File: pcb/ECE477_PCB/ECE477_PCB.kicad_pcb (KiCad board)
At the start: 2 copper layers, 65 x 30 mm, 102 parts, among them J1 DEBUG, J10 ToF 5, J11 Pi Zero, J2 USB_B_Micro, J3 ESC, J4 ELRS, J5 AUX_PWR, J6 ToF 1, J7 ToF 2, J8 ToF 3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

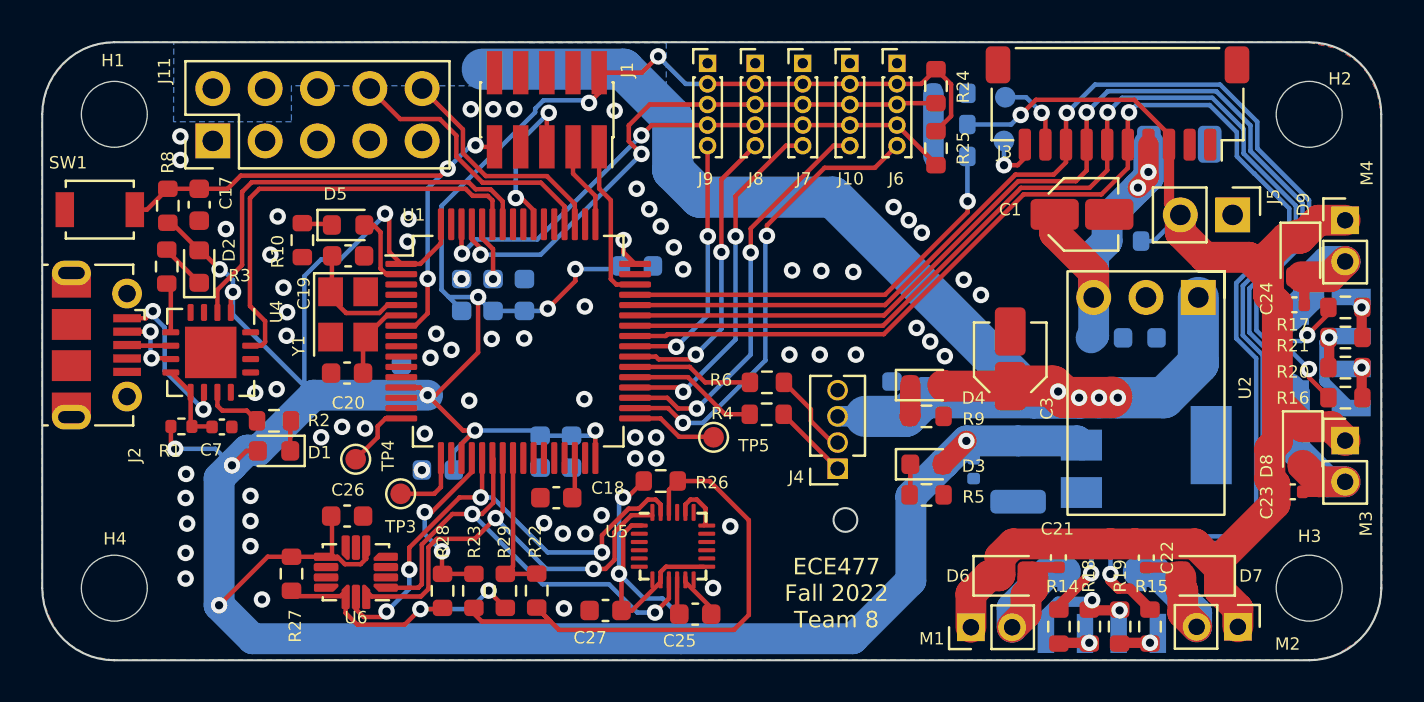
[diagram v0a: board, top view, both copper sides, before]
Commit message: committing before large change to FTDI
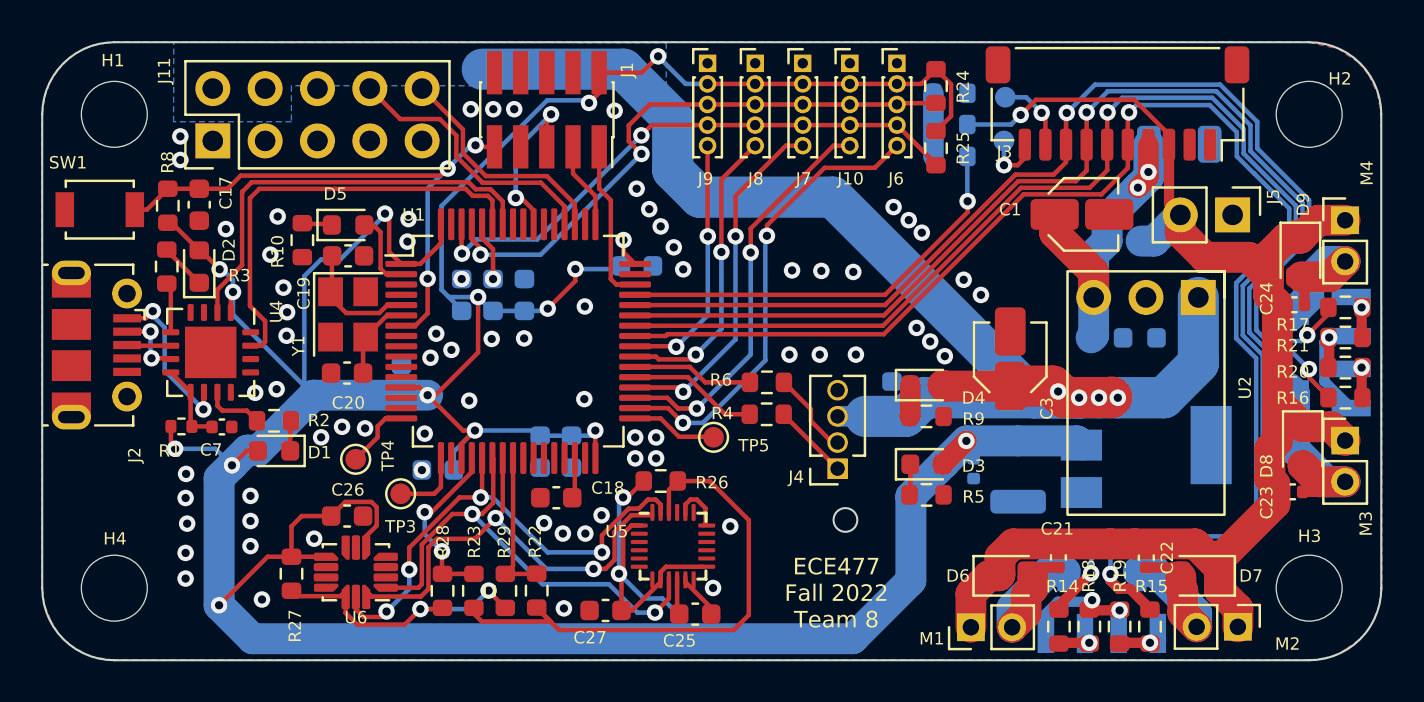
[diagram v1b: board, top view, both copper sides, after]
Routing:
- net +3V3: track 208.8 -> 213.2 mm
- net GND: vias 73 -> 74

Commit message: last fixes, ready to order (I think)
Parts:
- added C28: 1uF, Capacitor_SMD:C_0603_1608Metric, B.Cu at (94.7, 35.7)
- R11: value 10K -> 100K
- R12: value 220 -> 1K
- R13: value 100K -> 10K
- moved R1 0.35 mm to (54.7, 47.0)
- moved C7 0.32 mm to (56.6, 47.0)
- moved U4 0.22 mm to (56.3, 43.0)
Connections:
- U6 pad 2: unconnected-(U6-Pad2) -> +3V3
- U6 pad 3: unconnected-(U6-Pad3) -> +3V3
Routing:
- net GND: track 21.1 -> 24.8 mm
- net +3V3: track 213.2 -> 216.0 mm
- net VSENSE: track 20.5 -> 21.6 mm
- net VUSB: track 7.96 -> 8.81 mm
- net Net-(C7-Pad2): track 4.03 -> 4.82 mm
